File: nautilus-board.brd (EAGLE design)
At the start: 50.8 x 22.9 mm, 35 parts, among them Q3 DMG2305, SW1 KMR2, U1 2MB Flash, U2 AP2112(3.3V), U3 MCP73831T-2ACI/OT, X1 JSTPH, X2 4u20329

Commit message: Silkscreen update
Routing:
- net +3V3: track 62.6 -> 65.0 mm
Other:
- board text added: "D6"
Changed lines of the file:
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@@
 <text x="6.1722" y="2.7432" size="0.8128" layer="21" font="vector" ratio="20" align="center">rst</text>
 <text x="8.4328" y="2.794" size="1.016" layer="21" font="vector" ratio="20" rot="R180" align="center">3v</text>
-<text x="12.9032" y="2.7305" size="0.8128" layer="21" ratio="15" rot="R38.2" align="center">&lt;AR</text>
+<text x="12.9032" y="2.7305" size="0.8128" layer="21" font="vector" ratio="20" rot="R38.2" align="center">&lt;AR</text>
 <text x="18.6817" y="-1.4478" size="1.016" layer="21" ratio="15" align="center">G</text>
 <text x="15.5575" y="2.9845" size="1.016" layer="21" font="vector" ratio="20" rot="R180" align="center">GND</text>
-<text x="19.2151" y="2.9591" size="1.016" layer="21" font="vector" ratio="20" align="center">A1</text>
+<text x="19.2151" y="2.9591" size="1.016" layer="21" font="vector" ratio="20" align="center">D6</text>
 <text x="21.5392" y="2.9591" size="1.016" layer="21" font="vector" ratio="20" align="center">D5</text>
 <text x="24.1427" y="2.9591" size="1.016" layer="21" font="vector" ratio="20" rot="R180" align="center">D3</text>
 <text x="26.5938" y="2.9591" size="1.016" layer="21" font="vector" ratio="20" rot="R180" align="center">D2</text>
 <text x="29.0322" y="2.9591" size="1.016" layer="21" font="vector" ratio="20" align="center">D1</text>
-<text x="31.6992" y="2.9591" size="1.016" layer="21" ratio="20" align="center">SCK</text>
+<text x="31.6992" y="2.9591" size="1.016" layer="21" font="vector" ratio="20" align="center">SCK</text>
 <text x="34.3662" y="2.9591" size="1.016" layer="21" font="vector" ratio="20" rot="R180" align="center">SI</text>
 <text x="36.703" y="2.9591" size="1.016" layer="21" font="vector" ratio="20" align="center">SO</text>
@@
 <wire x1="19.8222" y1="8.7478" x2="19.7564" y2="8.682" width="0.4064" layer="1"/>
 <wire x1="17.907" y1="7.65629375" x2="17.907" y2="5.6134" width="0.4064" layer="1"/>
-<wire x1="17.907" y1="5.6134" x2="17.907" y2="2.9718" width="0.4064" layer="1"/>
+<wire x1="17.907" y1="5.6134" x2="17.907" y2="5.588" width="0.4064" layer="1"/>
+<wire x1="17.907" y1="5.588" x2="17.907" y2="2.9718" width="0.4064" layer="1"/>
 <wire x1="17.907" y1="2.9718" x2="17.4752" y2="2.54" width="0.4064" layer="16"/>
 <wire x1="17.4752" y1="2.54" x2="9.5758" y2="2.54" width="0.4064" layer="16"/>
@@
 <wire x1="20.3578" y1="5.4864" x2="18.034" y2="5.4864" width="0.254" layer="1"/>
 <wire x1="18.034" y1="5.4864" x2="17.907" y2="5.6134" width="0.254" layer="1"/>
-<wire x1="20.3578" y1="5.4864" x2="21.8948" y2="5.4864" width="0.254" layer="1"/>
-<wire x1="21.8948" y1="5.4864" x2="21.9964" y2="5.588" width="0.254" layer="1"/>
-<via x="21.9964" y="5.588" extent="1-16" drill="0.35"/>
 <via x="25.2222" y="7.366" extent="1-16" drill="0.35"/>
-<wire x1="21.9964" y1="5.588" x2="23.8915875" y2="5.588" width="0.254" layer="16"/>
 <wire x1="25.2222" y1="7.366" x2="25.2222" y2="6.9186125" width="0.254" layer="16"/>
 <wire x1="25.2222" y1="6.9186125" x2="23.8915875" y2="5.588" width="0.254" layer="16"/>
@@
 <wire x1="21.52538125" y1="12.8778" x2="21.83018125" y2="12.8778" width="0.4064" layer="1"/>
 <wire x1="21.83018125" y1="12.8778" x2="21.9964" y2="13.04401875" width="0.4064" layer="1"/>
+<via x="17.907" y="5.588" extent="1-16" drill="0.35"/>
+<wire x1="23.8915875" y1="5.588" x2="17.907" y2="5.588" width="0.254" layer="16"/>
 </signal>
 <signal name="VBAT" class="1">
@@
 <contactref element="Q3" pad="3"/>
 <contactref element="R12" pad="4"/>
-<wire x1="11.0236" y1="11.414" x2="11.0236" y2="14.0462" width="0.4064" layer="1"/>
-<wire x1="10.0838" y1="10.4742" x2="11.0236" y2="11.414" width="0.4064" layer="1"/>
+<wire x1="10.7442" y1="11.922" x2="10.7442" y2="13.7668" width="0.4064" layer="1"/>
+<wire x1="10.7442" y1="11.922" x2="10.0838" y2="11.2616" width="0.4064" layer="1"/>
+<wire x1="10.0838" y1="10.4742" x2="10.0838" y2="11.2616" width="0.4064" layer="1"/>
 <wire x1="12.8778" y1="16.637" x2="14.312" y2="18.0712" width="0.4064" layer="1"/>
 <wire x1="14.312" y1="18.0712" x2="16.5308" y2="18.0712" width="0.4064" layer="1"/>
@@
 <wire x1="14.409" y1="14.30915625" x2="14.417" y2="14.30115625" width="0.4064" layer="1"/>
 <wire x1="14.417" y1="14.30115625" x2="14.417" y2="12.9032" width="0.4064" layer="1"/>
-<wire x1="11.0236" y1="14.0462" x2="11.795" y2="14.8176" width="0.4064" layer="1"/>
+<wire x1="10.7442" y1="13.7668" x2="11.795" y2="14.8176" width="0.4064" layer="1"/>
 <wire x1="11.795" y1="14.8176" x2="11.795" y2="15.604" width="0.4064" layer="1"/>
 </signal>
@@
 <wire x1="35.258" y1="7.1402" x2="35.1536" y2="7.0358" width="0.2032" layer="1"/>
 <wire x1="36.4998" y1="9.779" x2="35.258" y2="8.5372" width="0.2032" layer="1"/>
-<wire x1="35.258" y1="8.5372" x2="35.258" y2="7.1402" width="0.2032" layer="1"/>
+<wire x1="35.258" y1="8.5372" x2="35.258" y2="8.255" width="0.2032" layer="1"/>
+<wire x1="35.258" y1="8.255" x2="35.258" y2="7.5692" width="0.2032" layer="1"/>
+<wire x1="35.258" y1="7.5692" x2="35.258" y2="7.1402" width="0.2032" layer="1"/>
 <wire x1="32.560090625" y1="6.733709375" x2="31.39710625" y2="6.733709375" width="0.2032" layer="1"/>
 <wire x1="31.39710625" y1="6.733709375" x2="28.87981875" y2="4.2164" width="0.2032" layer="1"/>
@@
 <wire x1="22.8346" y1="7.01043125" x2="22.8346" y2="4.572" width="0.2032" layer="1"/>
 <wire x1="22.8346" y1="4.572" x2="22.5171" y2="4.2545" width="0.2032" layer="1"/>
-<wire x1="22.5171" y1="4.2545" x2="22.5171" y2="3.7719" width="0.2032" layer="1"/>
-<wire x1="21.59" y1="2.8448" x2="22.5171" y2="3.7719" width="0.2032" layer="1"/>
+<wire x1="22.5171" y1="4.2545" x2="22.5171" y2="3.2639" width="0.2032" layer="1"/>
+<wire x1="22.5171" y1="3.2639" x2="22.225" y2="2.9718" width="0.2032" layer="1"/>
+<wire x1="22.225" y1="2.9718" x2="21.717" y2="2.9718" width="0.2032" layer="1"/>
+<wire x1="21.59" y1="2.8448" x2="21.717" y2="2.9718" width="0.2032" layer="1"/>
 <wire x1="23.8506" y1="8.02643125" x2="22.8346" y2="7.01043125" width="0.2032" layer="1"/>
 <via x="23.8252" y="8.9408" extent="1-16" drill="0.35"/>

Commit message: Adjusted traces
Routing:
- net RESET: track 33.8 -> 32.9 mm
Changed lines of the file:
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@@
 <drawing>
 <settings>
-<setting alwaysvectorfont="yes"/>
+<setting alwaysvectorfont="no"/>
 <setting verticaltext="up"/>
 </settings>
@@
 <wire x1="14.4018" y1="8.7989" x2="14.417" y2="8.7837" width="0.4064" layer="1"/>
 <via x="20.2184" y="20.1422" extent="1-16" drill="0.35"/>
-<wire x1="35.2898" y1="5.334" x2="35.2898" y2="4.0986" width="0.4064" layer="1"/>
-<wire x1="35.2898" y1="4.0986" x2="35.2806" y2="4.0894" width="0.4064" layer="1"/>
-<wire x1="35.306" y1="4.064" x2="35.306" y2="3.7592" width="0.4064" layer="1"/>
-<wire x1="35.306" y1="4.064" x2="35.2806" y2="4.0894" width="0.4064" layer="1"/>
+<wire x1="35.2898" y1="5.334" x2="35.306" y2="5.3178" width="0.4064" layer="1"/>
+<wire x1="35.306" y1="5.3178" x2="35.306" y2="3.7592" width="0.4064" layer="1"/>
 <via x="35.306" y="3.7592" extent="1-16" drill="0.35"/>
 <wire x1="20.2184" y1="20.1422" x2="20.32" y2="20.0406" width="0.4064" layer="1"/>
@@
 <wire x1="22.7428125" y1="4.5212" x2="17.2851" y2="4.5212" width="0.254" layer="16"/>
 <wire x1="17.2851" y1="4.5212" x2="16.8148" y2="4.0509" width="0.254" layer="16"/>
-<wire x1="34.0198" y1="5.334" x2="34.0198" y2="3.9208" width="0.2032" layer="1"/>
-<wire x1="34.0198" y1="3.9208" x2="33.7606875" y2="3.9208" width="0.2032" layer="1"/>
-<wire x1="33.7606875" y1="3.9208" x2="33.1602875" y2="4.5212" width="0.2032" layer="1"/>
-<wire x1="33.1602875" y1="4.5212" x2="30.0736" y2="4.5212" width="0.2032" layer="1"/>
+<wire x1="34.0198" y1="5.334" x2="34.0198" y2="4.5212" width="0.2032" layer="1"/>
+<wire x1="34.0198" y1="4.5212" x2="30.0736" y2="4.5212" width="0.2032" layer="1"/>
 <wire x1="30.0736" y1="4.5212" x2="29.4894" y2="3.937" width="0.2032" layer="1"/>
 <wire x1="29.4894" y1="3.8608" x2="29.4894" y2="3.937" width="0.2032" layer="1"/>
@@
 <contactref element="U1" pad="5"/>
 <wire x1="28.87981875" y1="4.2164" x2="26.9878" y2="4.2164" width="0.2032" layer="1"/>
-<wire x1="35.1536" y1="7.0358" x2="32.86218125" y2="7.0358" width="0.2032" layer="1"/>
 <wire x1="32.86218125" y1="7.0358" x2="32.560090625" y2="6.733709375" width="0.2032" layer="1"/>
 <wire x1="38.4648" y1="7.634" x2="38.4648" y2="9.4742" width="0.2032" layer="1"/>
-<wire x1="35.258" y1="7.1402" x2="35.1536" y2="7.0358" width="0.2032" layer="1"/>
-<wire x1="36.4998" y1="9.779" x2="35.258" y2="8.5372" width="0.2032" layer="1"/>
-<wire x1="35.258" y1="8.5372" x2="35.258" y2="8.255" width="0.2032" layer="1"/>
-<wire x1="35.258" y1="8.255" x2="35.258" y2="7.5692" width="0.2032" layer="1"/>
-<wire x1="35.258" y1="7.5692" x2="35.258" y2="7.1402" width="0.2032" layer="1"/>
 <wire x1="32.560090625" y1="6.733709375" x2="31.39710625" y2="6.733709375" width="0.2032" layer="1"/>
 <wire x1="31.39710625" y1="6.733709375" x2="28.87981875" y2="4.2164" width="0.2032" layer="1"/>
 <wire x1="38.4648" y1="9.4742" x2="38.16" y2="9.779" width="0.2032" layer="1"/>
-<wire x1="38.16" y1="9.779" x2="36.4998" y2="9.779" width="0.2032" layer="1"/>
+<wire x1="38.16" y1="9.779" x2="36.4744" y2="9.779" width="0.2032" layer="1"/>
+<wire x1="35.2566" y1="7.5678" x2="34.7246" y2="7.0358" width="0.2032" layer="1"/>
+<wire x1="34.7246" y1="7.0358" x2="32.86218125" y2="7.0358" width="0.2032" layer="1"/>
+<wire x1="35.2566" y1="8.5612" x2="35.2566" y2="7.5678" width="0.2032" layer="1"/>
+<wire x1="36.4744" y1="9.779" x2="35.2566" y2="8.5612" width="0.2032" layer="1"/>
 </signal>
 <signal name="SPI_FLASH_CS_PIN">
@@
 <wire x1="7.7216" y1="7.8486" x2="7.874" y2="8.001" width="0.254" layer="16"/>
 <via x="33.02" y="5.7912" extent="1-16" drill="0.35"/>
-<wire x1="36.2712" y1="6.6294" x2="33.1216" y2="6.6294" width="0.254" layer="1"/>
-<wire x1="33.1216" y1="6.6294" x2="33.02" y2="6.5278" width="0.254" layer="1"/>
-<wire x1="33.02" y1="6.5278" x2="33.02" y2="5.7912" width="0.254" layer="1"/>
+<wire x1="36.2712" y1="6.6294" x2="33.528" y2="6.6294" width="0.254" layer="1"/>
 <wire x1="36.5598" y1="5.334" x2="36.5598" y2="6.3408" width="0.254" layer="1"/>
-<wire x1="36.5598" y1="6.3408" x2="36.2712" y2="6.6294" width="0.254" layer="1"/>
+<wire x1="36.2712" y1="6.6294" x2="36.5598" y2="6.3408" width="0.254" layer="1"/>
 <wire x1="23.8252" y1="4.9276" x2="25.7556" y2="6.858" width="0.2032" layer="16"/>
 <wire x1="25.7556" y1="6.858" x2="32.5882" y2="6.858" width="0.2032" layer="16"/>
@@
 <wire x1="12.4206" y1="8.001" x2="15.494" y2="4.9276" width="0.254" layer="16"/>
 <wire x1="15.494" y1="4.9276" x2="23.8252" y2="4.9276" width="0.254" layer="16"/>
+<wire x1="33.528" y1="6.6294" x2="33.512" y2="6.6134" width="0.254" layer="1"/>
+<wire x1="33.512" y1="6.6134" x2="33.50406875" y2="6.6134" width="0.254" layer="1"/>
+<wire x1="33.50406875" y1="6.6134" x2="33.02" y2="6.12933125" width="0.254" layer="1"/>
+<wire x1="33.02" y1="6.12933125" x2="33.02" y2="5.7912" width="0.254" layer="1"/>
 </signal>
 <signal name="D+1">
@@
 <via x="42.2402" y="9.8806" extent="1-16" drill="0.35"/>
 <via x="36.5948" y="3.8034" extent="1-16" drill="0.35"/>
-<wire x1="32.62275" y1="3.8354" x2="30.05735" y2="1.27" width="0.2032" layer="1"/>
+<wire x1="32.52115" y1="3.7338" x2="30.05735" y2="1.27" width="0.2032" layer="1"/>
 <wire x1="29.21" y1="1.27" x2="30.05735" y2="1.27" width="0.2032" layer="1"/>
-<wire x1="32.62275" y1="3.8354" x2="33.30726875" y2="3.8354" width="0.2032" layer="1"/>
+<wire x1="32.52115" y1="3.7338" x2="33.40886875" y2="3.7338" width="0.2032" layer="1"/>
 <wire x1="35.65653125" y1="2.86513125" x2="36.5948" y2="3.8034" width="0.2032" layer="1"/>
 <wire x1="34.2775375" y1="2.86513125" x2="35.65653125" y2="2.86513125" width="0.2032" layer="1"/>
-<wire x1="33.30726875" y1="3.8354" x2="34.2775375" y2="2.86513125" width="0.2032" layer="1"/>
+<wire x1="33.40886875" y1="3.7338" x2="34.2775375" y2="2.86513125" width="0.2032" layer="1"/>
 <wire x1="42.2402" y1="9.8806" x2="42.2402" y2="7.8232" width="0.2032" layer="16"/>
 <wire x1="42.2402" y1="7.8232" x2="38.8366" y2="4.4196" width="0.2032" layer="16"/>

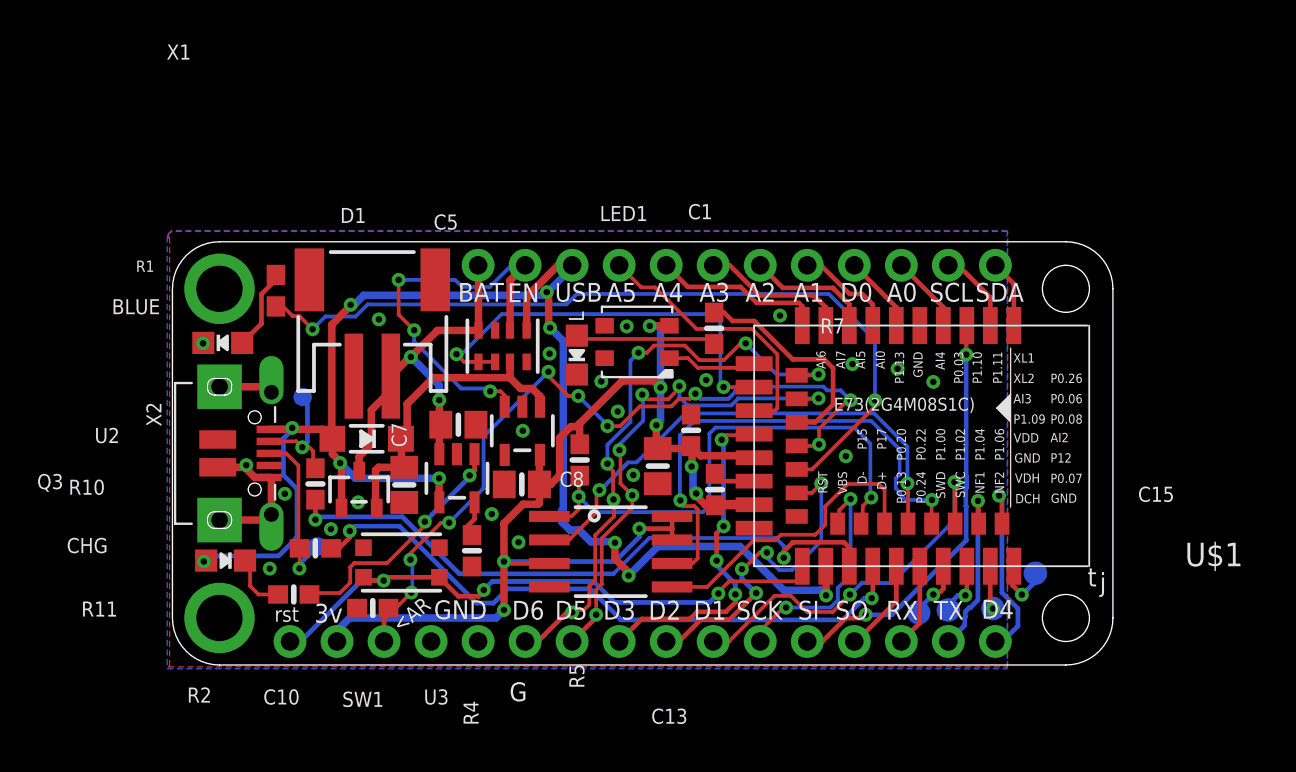
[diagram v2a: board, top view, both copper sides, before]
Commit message: External XTAL
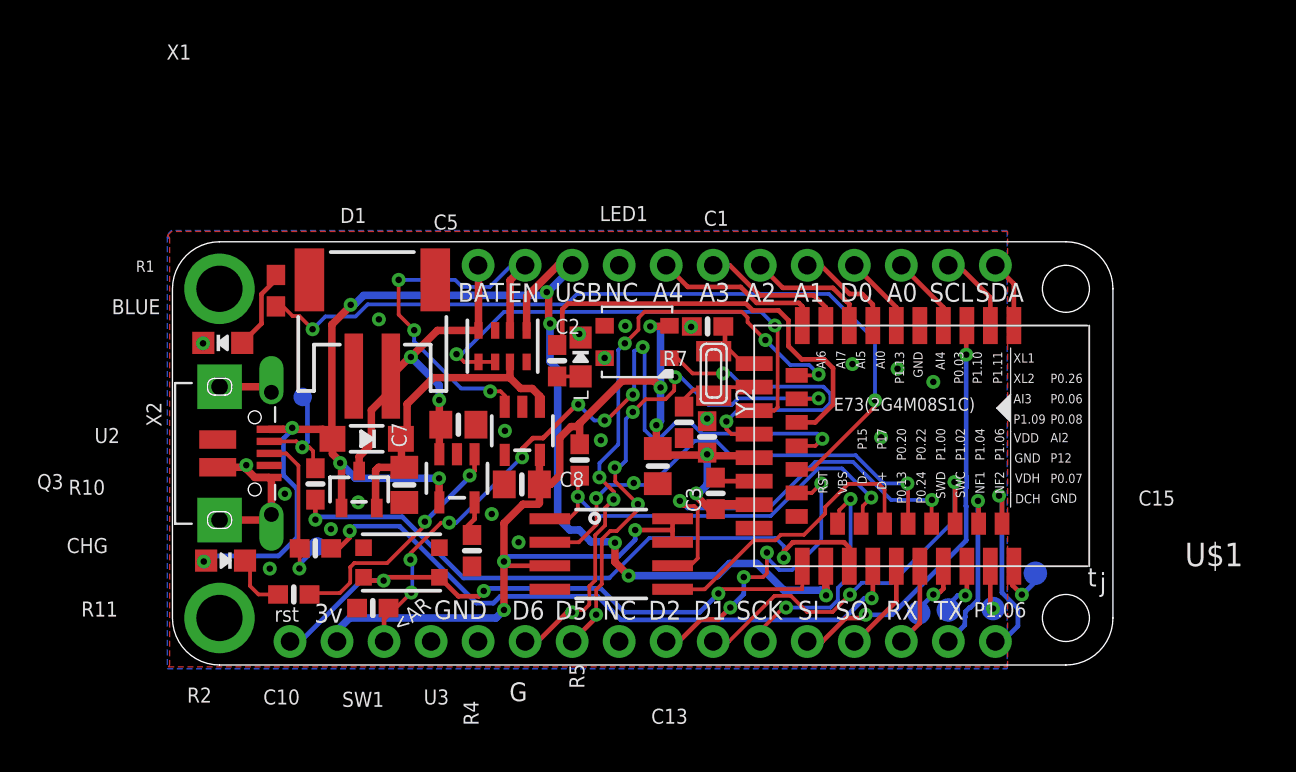
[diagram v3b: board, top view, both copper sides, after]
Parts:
- added C2, C3: 22pF, microbuilder:0603-NO
- added Y2: 32.768, adafruit2:XTAL3215
- moved R7 8.66 mm to (20.8, 16.4)
- moved C1 0.93 mm to (28.9, 12.3)
- moved L 0.23 mm to (22.0, 16.6), turned to 0 degrees
- moved C15 0.20 mm to (29.3, 9.27)
- moved U1 0.13 mm to (23.7, 5.99)
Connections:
- removed net A5: MS1.25, U$1.15
- new net N$2: C3.1, U$1.13, Y2.P$2
- new net N$7: C2.1, U$1.11, Y2.P$1
- net D2: no longer MS1.9
- net D3: no longer U$1.17
- net GND: now also C2.2, C3.2
- net NEOPIXEL: now also U$1.17; no longer U$1.11
- net VDIV: now also U$1.15; no longer U$1.13
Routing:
- net D3: track 18.4 -> 0.00 mm, vias 4 -> 0
- net A5: track 14.8 -> 0.00 mm
- net NEOPIXEL: track 4.89 -> 18.0 mm, vias 0 -> 2
- net LED_RED: track 12.0 -> 23.4 mm
- net N$3: track 7.60 -> 1.27 mm
- net SPI_FLASH_CS_PIN: track 28.8 -> 23.3 mm
- net SPI_FLASH_SCK_PIN: track 27.5 -> 22.3 mm
- net N$2: track 0.00 -> 4.73 mm
- net N$7: track 0.00 -> 3.82 mm
- net VDIV: track 22.8 -> 26.5 mm
- net D6: track 31.8 -> 34.2 mm
- net SPI_FLASH_MISO_PIN: track 27.7 -> 25.6 mm
- net D2: track 18.1 -> 16.7 mm
- net VBUS: track 85.1 -> 84.3 mm
- net AREF: track 44.1 -> 43.3 mm
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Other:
- board text added: "NC"
- board text added: "P1.06"
- board text removed: "A5"
- board text removed: "D3"
- board text removed: "D4"

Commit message: Adjustments
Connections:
- removed net D3: MS1.8
- removed net D6: MS1.6, U$1.12
- new net P1.06: MS1.16, U$1.42
- net D2: now also MS1.9
- net D4: now also MS1.7, U$1.14; no longer MS1.16, U$1.42
- net D5: now also MS1.6, U$1.12; no longer MS1.7, U$1.14
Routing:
- net D6: track 34.2 -> 0.00 mm, vias 6 -> 0
- net D4: track 10.7 -> 28.3 mm, vias 1 -> 6
- net P1.06: track 0.00 -> 10.7 mm, vias 0 -> 1
- net D5: track 28.3 -> 34.2 mm
- net AREF: track 43.3 -> 38.0 mm, vias 9 -> 8
- net VBUS: track 84.3 -> 85.5 mm
- net +3V3: track 65.1 -> 66.0 mm
- net D2: track 16.7 -> 17.4 mm
- net USBD-: track 34.7 -> 34.1 mm
- net GND: vias 21 -> 23
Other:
- board text added: "1.06"
- board text removed: "P1.06"

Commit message: Add files via upload
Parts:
- moved C2 0.33 mm to (29.2, 18.3)
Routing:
- net GND: track 13.3 -> 15.3 mm
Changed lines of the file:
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@@
 <drawing>
 <settings>
-<setting alwaysvectorfont="yes"/>
+<setting alwaysvectorfont="no"/>
 <setting verticaltext="up"/>
 </settings>
@@
 <attribute name="VALUE" x="26.359" y="28.1594" size="1.016" layer="27" font="vector" rot="R90"/>
 </element>
-<element name="C2" library="microbuilder" package="0603-NO" value="22pF" x="28.9052" y="18.288" smashed="yes" rot="R180">
-<attribute name="NAME" x="22.0218" y="18.6944" size="0.8128" layer="25" font="vector" ratio="18" rot="R180"/>
-<attribute name="VALUE" x="5.4356" y="19.4056" size="0.4064" layer="27" font="vector" ratio="10" rot="R180"/>
+<element name="C2" library="microbuilder" package="0603-NO" value="22pF" x="29.2354" y="18.3134" smashed="yes" rot="R180">
+<attribute name="NAME" x="22.352" y="18.7198" size="0.8128" layer="25" font="vector" ratio="18" rot="R180"/>
+<attribute name="VALUE" x="5.7658" y="19.431" size="0.4064" layer="27" font="vector" ratio="10" rot="R180"/>
 </element>
 <element name="C3" library="microbuilder" package="0603-NO" value="22pF" x="27.6352" y="13.1064" smashed="yes" rot="R270">
@@
 <via x="23.3426" y="16.5862" extent="1-16" drill="0.35"/>
 <via x="28.8798" y="13.3096" extent="1-16" drill="0.35"/>
-<via x="28.0162" y="18.2626" extent="1-16" drill="0.35"/>
+<via x="28.3464" y="18.3388" extent="1-16" drill="0.35"/>
 <via x="29.0576" y="5.9182" extent="1-16" drill="0.35"/>
 <via x="22.0726" y="4.8006" extent="1-16" drill="0.35"/>
+<wire x1="28.3854" y1="18.3134" x2="27.9806" y2="17.9086" width="0.3048" layer="1"/>
+<wire x1="27.9806" y1="17.9086" x2="27.9806" y2="16.435725" width="0.3048" layer="1"/>
 </signal>
 <signal name="VBUS" class="1">
@@
 <wire x1="29.845" y1="17.0664" x2="29.3538" y2="17.0664" width="0.2032" layer="1"/>
 <wire x1="29.3538" y1="17.0664" x2="29.2354" y2="16.948" width="0.2032" layer="1"/>
-<wire x1="29.7552" y1="18.288" x2="29.845" y2="18.1982" width="0.254" layer="1"/>
-<wire x1="29.845" y1="18.1982" x2="29.845" y2="17.0664" width="0.254" layer="1"/>
+<wire x1="30.0854" y1="18.3134" x2="29.845" y2="18.073" width="0.254" layer="1"/>
+<wire x1="29.845" y1="18.073" x2="29.845" y2="17.0664" width="0.254" layer="1"/>
 </signal>
 <signal name="N$2">
